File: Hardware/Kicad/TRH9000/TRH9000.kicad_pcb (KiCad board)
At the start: 4 copper layers, 99.1 x 63.5 mm, 64 parts, among them J1 RGB, Q1 BC817, U1 V9990, U2 KM428C256, U3 KM428C256, U4 74HC138, U6 LMH1980, U7 74HC32, X1 14.31818MHz, Y1 21.47727Mhz

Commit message: Multiple changes. Check the dev log.
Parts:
- added J2: RGB, Connector_Dsub:DSUB-15-HD_Female_Horizontal_P2.29x1.98mm_EdgePinOffset3.03mm_Housed_MountingHolesOffset4.94mm, F.Cu at (134.5, 57.1)
- added SW1: SW_DP3T, Switches:SWITCH_SP3T_SMD, F.Cu at (111.0, 51.8)
- added U7: ICL7660, Package_SO:SOP-8_3.9x4.9mm_P1.27mm, F.Cu at (105.8, 59.1)
- added U8: LT1675, Package_SO:SSOP-16_3.9x4.9mm_P0.635mm, F.Cu at (117.0, 59.3)
- moved J1 13.8 mm to (173.6, 57.1)
- moved C27 1.47 mm to (108.5, 87.1)
- moved C26 1.45 mm to (103.9, 87.1)
- moved C24 1.18 mm to (103.9, 66.8)
- moved C25 1.13 mm to (108.3, 66.8)
- moved Y1 0.60 mm to (191.3, 91.2)
- renumbered C10 to C1, C33 to C10, C34 to C11, C19 to C12, C20 to C13, C21 to C14, C13 to C15, C35 to C16, C36 to C17, C28 to C18, C29 to C19, C27 to C2, C30 to C20, C31 to C21, C2 to C22, C3 to C23, C5 to C24, C6 to C25, C7 to C26, C8 to C27, C1 to C3, C17 to C5, C14 to C6, C15 to C7, C16 to C8, C32 to C9, L3 to L1, L1 to L2, L2 to L3, R5 to R1, R9 to R10, R10 to R11, R24 to R12, R25 to R13, R26 to R14, R17 to R15, R18 to R16, R19 to R17, R3 to R2, R6 to R3, R1 to R5, R2 to R6, R12 to R7, R13 to R8, R15 to R9, U4 to U1, U7 to U2, U1 to U3, U3 to U4, U2 to U5
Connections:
- BUS1 pad 48: +12V -> unconnected-(BUS1-Pad48)
- BUS1 pad 50: -12V -> unconnected-(BUS1-Pad50)
- U3 pad 2: /VDP/~{VDPR} -> /VDP/~{VDPW}
- U3 pad 3: /VDP/~{VDPW} -> /VDP/~{VDPR}
- U4 pad 13: unconnected-(U3-Pad13) (its old number) -> GND
- U4 pad 21: unconnected-(U3-Pad21) -> GND
- U5 pad 13: unconnected-(U2-Pad13) -> GND
- U5 pad 21: unconnected-(U2-Pad21) -> GND
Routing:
- net /VIDEO/ROUT: track 5.78 -> 21.2 mm
- net /VIDEO/BOUT: track 14.5 -> 29.5 mm
- net GND: track 135.9 -> 150.9 mm, vias 33 -> 36
- net /VIDEO/GOUT: track 8.96 -> 23.8 mm
- net GND1: track 26.0 -> 40.8 mm
- net GNDA: track 119.2 -> 129.7 mm, vias 2 -> 3
- net +5VA: track 78.6 -> 69.0 mm
- net /VDP/~{VDPW}: track 42.5 -> 51.8 mm, vias 3 -> 1
- net /VIDEO/VSYNC: track 42.9 -> 50.1 mm
- net /VIDEO/HSYNC: track 39.6 -> 46.2 mm
- net /VDP/~{VDPR}: track 44.8 -> 51.2 mm, vias 3 -> 1
- net +5V: track 96.0 -> 100.9 mm
- net /A2: track 69.0 -> 71.8 mm
- net /A1: track 66.3 -> 69.0 mm
- net /VDP/~{V0_WE}: track 44.6 -> 47.0 mm
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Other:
- board size 99.1 x 63.5 mm -> 99.1 x 77.2 mm
- board text added: "The Yamaha V9990 open-source video card for the MSX Rev 2"
- board text removed: "The Yamaha V9990 open-source video card for the MSX Rev 1"

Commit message: Multiple changes.
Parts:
- removed Cart1: MSX-cartridge_dummy, trh9000:MSX-cart-dummy
- removed J2: RGB, Connector_Dsub:DSUB-15-HD_Female_Horizontal_P2.29x1.98mm_EdgePinOffset3.03mm_Housed_MountingHolesOffset4.94mm
- removed SW1: SW_DP3T, Switches:SWITCH_SP3T_SMD
- removed U7: ICL7660, Package_SO:SOP-8_3.9x4.9mm_P1.27mm
- removed U8: LT1675, Package_SO:SSOP-16_3.9x4.9mm_P0.635mm
- C15, C22, C3, C4, L2, L3, R1, R15, R16, R17, R2, R3, R4, R5, R6: moved to B.Cu
- C16: footprint Capacitor_SMD:C_0805_2012Metric_Pad1.18x1.45mm_HandSolder -> Capacitor_SMD:C_0805_2012Metric
- C23: footprint Capacitor_SMD:C_0805_2012Metric -> Capacitor_THT:CP_Radial_D5.0mm_P2.50mm
- L1: footprint Inductor_SMD:L_0805_2012Metric -> Inductor_SMD:L_1206_3216Metric
- MSX1, TRH1: renamed from G***; moved to F.Cu
- moved C24 103.2 mm to (202.2, 98.2), turned to -90 degrees
- moved C25 100.8 mm to (202.3, 103.4), turned to -90 degrees
- moved C26 98.7 mm to (202.2, 79.4), turned to -90 degrees
- moved C27 93.8 mm to (202.2, 84.9), turned to -90 degrees
- moved X1 78.8 mm to (117.0, 82.7), turned to 0 degrees
- moved Y1 72.7 mm to (123.1, 65.8)
- moved U4 72.6 mm to (183.3, 97.0)
- moved U5 71.9 mm to (183.3, 78.8)
- moved C4 68.7 mm to (117.0, 57.9)
- moved C3 65.5 mm to (123.9, 57.9)
- moved R2 55.1 mm to (134.3, 64.5), turned to 90 degrees
- moved Q1 50.5 mm to (144.3, 71.2), turned to 0 degrees
- moved L2 48.6 mm to (126.7, 95.0), turned to 0 degrees
- moved R9 47.5 mm to (144.5, 64.5), turned to 90 degrees
- moved C8 46.4 mm to (204.8, 83.2)
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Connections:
- U1 pad 1: /A4 -> /A3
- U1 pad 4: /~{IORQ} -> /A4
- U1 pad 9: Net-(U1-Pad9) -> Net-(U2-Pad4)
- U2 pad 1: /~{RD} -> Net-(U2-Pad1)
- U2 pad 10: /SYS_CLK -> Net-(U2-Pad1)
- U2 pad 11: /~{BUSDIR} -> /VDP/~{VDPR}
- U2 pad 12: Net-(U1-Pad9) -> Net-(U2-Pad1)
- U2 pad 2: Net-(U1-Pad9) -> /~{WR}
- U2 pad 3: /VDP/~{VDPR} -> /VDP/~{VDPW}
- U2 pad 4: /~{WR} -> Net-(U2-Pad4)
- U2 pad 5: Net-(U1-Pad9) -> /~{IORQ}
- U2 pad 6: /VDP/~{VDPW} -> Net-(U2-Pad1)
- U2 pad 8: /SCIN -> /~{BUSDIR}
- U2 pad 9: /SYS_CLK -> /~{RD}
- U4 pad 12: /VDP/~{V0_WE} -> GND
- U4 pad 13: GND -> /VDP/~{V0_WE}
- U5 pad 12: /VDP/~{V1_WE} -> GND
- U5 pad 13: GND -> /VDP/~{V1_WE}
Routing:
- net +5VA: track 69.0 -> 139.4 mm, vias 3 -> 0
- net /VDP/B: track 9.89 -> 71.1 mm
- net /VDP/G: track 12.7 -> 63.6 mm
- net /~{RESET}: track 47.0 -> 94.2 mm
- net /~{IORQ}: track 21.8 -> 68.8 mm
- net /SYS_CLK: track 42.2 -> 0.00 mm, vias 1 -> 0
- net /VDP/V0A3: track 64.2 -> 23.5 mm
- net GND: track 150.9 -> 111.6 mm, vias 36 -> 34
- net /VDP/V0A2: track 62.9 -> 23.9 mm
- net /VDP/R: track 17.4 -> 55.2 mm
- net /VDP/V0A1: track 62.2 -> 24.4 mm
- net /VDP/V0A0: track 61.4 -> 24.9 mm
- net /D6: track 76.7 -> 42.1 mm, vias 2 -> 0
- net /VDP/V1D7: track 44.8 -> 78.5 mm
- net /A2: track 71.8 -> 38.2 mm
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- added copper zone on In1.Cu, net +5V
- added copper zone on In2.Cu, net GND
- removed copper zone on In2.Cu, net +5V
- removed copper zone on In1.Cu, net GND
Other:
- board size 99.1 x 77.2 mm -> 100.1 x 73.4 mm
- board text added: "The Yamaha V9990 open-source video card for the MSX Rev 0.3"
- board text removed: "Designed by the MSX community for the MSX community."
- board text removed: "The Yamaha V9990 open-source video card for the MSX Rev 2"

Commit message: Minor adjustments
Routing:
- net /VDP/V1S0: track 38.8 -> 39.8 mm
- net /VDP/~{V0_RAS}: track 20.5 -> 21.5 mm
- net /VDP/V1S1: track 36.6 -> 37.5 mm
- net /VDP/V0A8: track 35.9 -> 36.9 mm
- net /VDP/~{V0_WE}: track 21.3 -> 22.2 mm
- net /VDP/~{V1_SC}: track 49.2 -> 50.1 mm
- net +5VA: track 139.4 -> 140.2 mm
- net /VDP/V1S4: track 31.9 -> 32.7 mm
- net /VDP/V1D1: track 46.0 -> 46.7 mm
- net /VDP/~{V1_SOE}: track 42.6 -> 43.3 mm
- net /VDP/V1S7: track 37.3 -> 38.0 mm
- net /VDP/V0A7: track 33.7 -> 34.4 mm
- net /VDP/V1D0: track 50.4 -> 51.0 mm
- net /VDP/V1D3: track 46.3 -> 46.9 mm
- net /VDP/V1D7: track 78.5 -> 79.1 mm
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
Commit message: Multiple changes.
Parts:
- added REF**: OSHW-Logo2_9.8x8mm_SilkScreen, Symbol:OSHW-Logo2_9.8x8mm_SilkScreen, B.Cu at (182.4, 94.2)
- C11, C17: value 0.1µF -> 0.1uF
- C12, C13, C14: footprint Capacitor_THT:CP_Radial_D5.0mm_P2.50mm -> Capacitor_Tantalum_SMD:CP_EIA-3528-15_AVX-H; moved to B.Cu
- C15: value 10µF -> 10uF
- C18, C20: value 1 µF -> 1uF
- C2: value 1 µF -> 10uF
- C22: moved to F.Cu
- C23: footprint Capacitor_THT:CP_Radial_D5.0mm_P2.50mm -> Capacitor_Tantalum_SMD:CP_EIA-3528-15_AVX-H
- C5: value 220uF -> 220uF 6.3V; footprint Capacitor_THT:CP_Radial_D5.0mm_P2.50mm -> Capacitor_Tantalum_SMD:CP_EIA-3528-15_AVX-H; moved to B.Cu
- L1: value 4.7µH -> 4.7uH; footprint Inductor_SMD:L_1206_3216Metric -> Inductor_SMD:L_0805_2012Metric
- L2, L3: footprint Inductor_SMD:L_1206_3216Metric -> Inductor_SMD:L_0805_2012Metric; moved to F.Cu
- R12: value 10k -> 10K; footprint Capacitor_SMD:C_0805_2012Metric -> Resistor_SMD:R_0805_2012Metric
- moved MSX1 94.1 mm to (194.3, 114.6)
- moved RV3 70.3 mm to (126.2, 82.5), turned to 180 degrees
- moved RV2 56.4 mm to (133.3, 82.5), turned to 180 degrees
- moved TRH1 56.3 mm to (118.9, 113.5)
- moved C12 48.4 mm to (141.3, 71.9), turned to 180 degrees
- moved C13 47.5 mm to (149.0, 71.9), turned to 180 degrees
- moved C14 46.7 mm to (156.7, 71.9), turned to 180 degrees
- moved RV1 42.0 mm to (140.7, 82.5), turned to 180 degrees
- moved C6 41.4 mm to (148.9, 83.1)
- moved R17 41.4 mm to (163.5, 78.0)
- moved R15 41.4 mm to (148.9, 78.0)
- moved C8 41.3 mm to (163.5, 83.1)
- moved R16 41.3 mm to (156.3, 78.0)
- moved C7 41.2 mm to (156.3, 83.1)
- moved C10 40.5 mm to (191.0, 83.1), turned to 0 degrees
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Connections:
- BUS1 pad 12: /~{MERQ} -> unconnected-(BUS1-Pad12)
- C10 pad 1: Net-(C10-Pad1) -> Net-(C11-Pad1)
- C11 pad 1: /VIDEO/SYNCIN -> Net-(C11-Pad1)
- C11 pad 2: Net-(C10-Pad1) -> /VIDEO/SYNCIN
- C15 pad 1: GND -> GND1
- C15 pad 2: GND1 -> GND
- C16 pad 1: +5VA -> GND
- C16 pad 2: GND -> +5VA
- C9 pad 1: Net-(C10-Pad1) -> Net-(C11-Pad1)
- R11 pad 1: Net-(C10-Pad1) -> Net-(C11-Pad1)
- R12 pad 1: GND -> Net-(R12-Pad1)
- R12 pad 2: Net-(R12-Pad2) -> GND
- U6 pad 1: Net-(R12-Pad2) -> Net-(R12-Pad1)
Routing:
- net /VDP/V1D2: track 53.0 -> 163.8 mm, vias 0 -> 6
- net /VDP/V1S3: track 41.3 -> 147.2 mm, vias 0 -> 6
- net /VDP/V0S0: track 36.7 -> 126.1 mm, vias 0 -> 8
- net /VDP/V1D6: track 54.1 -> 141.0 mm, vias 2 -> 4
- net /VDP/V1A2: track 32.5 -> 114.4 mm, vias 2 -> 0
- net /VDP/~{V0_WE}: track 22.2 -> 91.6 mm, vias 0 -> 6
- net /VDP/~{VDPW}: track 24.4 -> 93.7 mm, vias 1 -> 5
- net /VDP/V1D1: track 46.7 -> 114.2 mm, vias 0 -> 6
- net /VDP/B: track 71.1 -> 4.41 mm
- net /VDP/V1S7: track 38.0 -> 100.3 mm, vias 0 -> 4
- net /VDP/G: track 63.6 -> 6.62 mm
- net Net-(C5-Pad1): track 57.2 -> 9.95 mm
- net /VDP/~{V1_RAS}: track 20.0 -> 64.7 mm, vias 0 -> 4
- net Net-(C5-Pad2): track 50.1 -> 5.42 mm
- net /VDP/V1D5: track 52.3 -> 96.2 mm, vias 2 -> 4
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- added copper zone on In2.Cu, net +5V
- added copper zone on In1.Cu, net GND
- removed copper zone on In1.Cu, net +5V
- removed copper zone on In2.Cu, net GND
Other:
- board size 100.1 x 73.4 mm -> 100 x 77.5 mm
- board text added: "The Yamaha V9990 open-source video card for the MSX Rev 1.0"
- board text removed: "The Yamaha V9990 open-source video card for the MSX Rev 0.3"

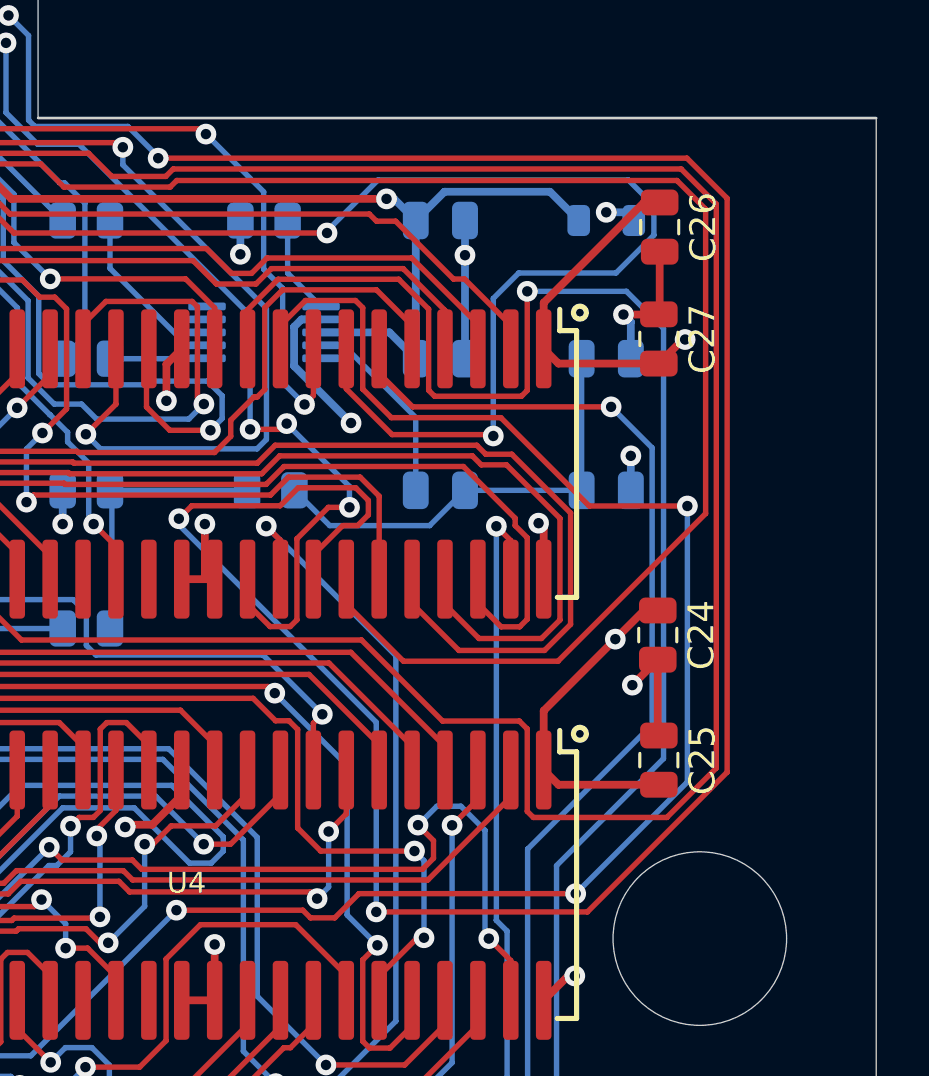
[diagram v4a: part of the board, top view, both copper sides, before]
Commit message: Moving caps to avoid conflict with sockets, uploading image with issue when superimposing
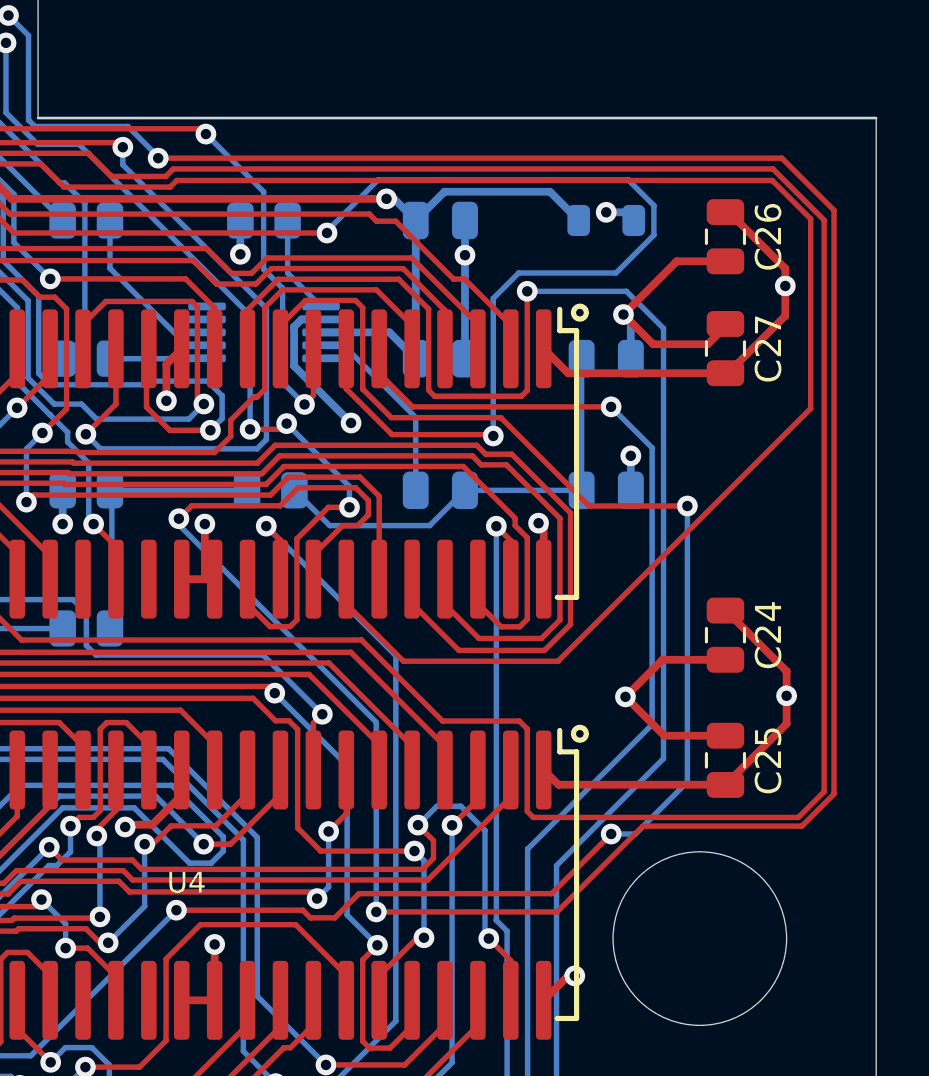
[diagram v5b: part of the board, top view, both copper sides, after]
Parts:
- C5: value 220uF 6.3V -> 220uF
- moved C24 2.61 mm to (195.6, 88.7)
- moved C27 2.60 mm to (195.6, 77.6)
- moved C25 2.57 mm to (195.6, 93.5)
- moved C26 2.57 mm to (195.6, 73.3)
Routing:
- net GND: track 109.4 -> 120.0 mm
- net /VDP/V1A2: track 114.4 -> 122.9 mm
- net /VDP/V1D6: track 141.0 -> 149.5 mm
- net /VDP/V1D7: track 103.5 -> 109.0 mm
- net +5V: track 84.1 -> 88.7 mm
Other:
- board text added: "+"
